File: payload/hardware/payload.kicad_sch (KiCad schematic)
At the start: 4 parts, among them J1 522071585, J2 Conn_01x05, U1 CM4102008, U3 CD74HC4067SM

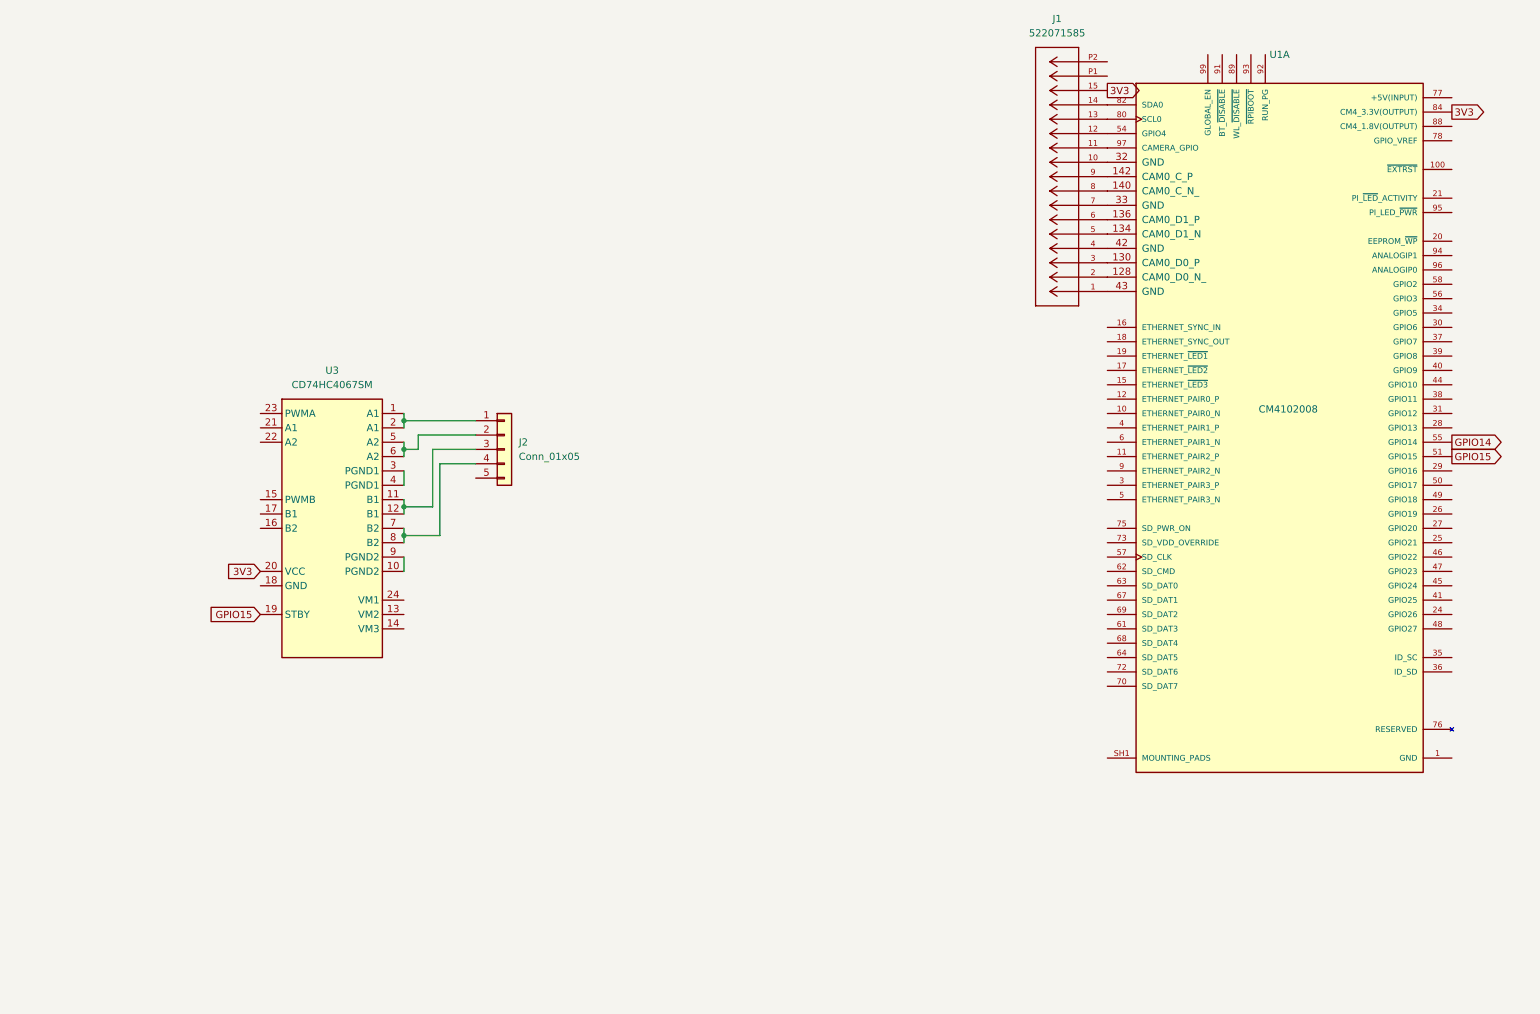
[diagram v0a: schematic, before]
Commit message: interboard connector and organization
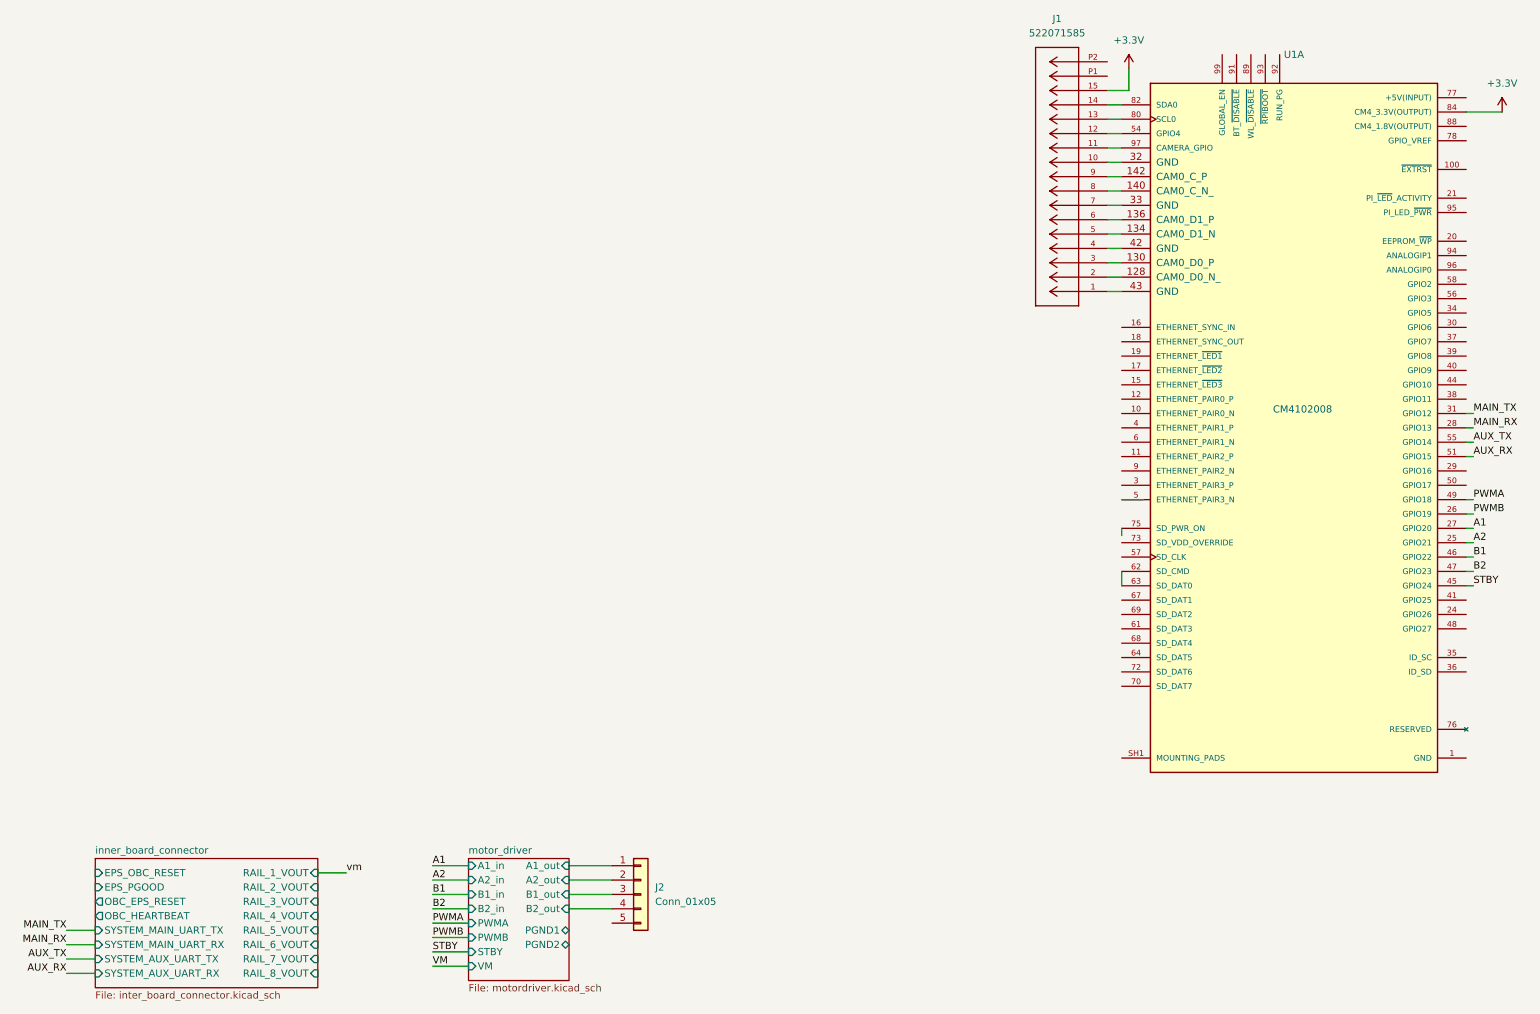
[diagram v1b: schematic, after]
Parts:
- removed U3: CD74HC4067SM, Package_SO:SSOP-24_5.3x8.2mm_P0.65mm, symbol 74xx:CD74HC4067SM
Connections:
- net motor_driver/A1_out: now reaches J2.1 (Pin_1)
- net motor_driver/B1_out: now reaches J2.3 (Pin_3)
- net motor_driver/A2_out: now reaches J2.2 (Pin_2)
- net motor_driver/B2_out: now reaches J2.4 (Pin_4)
- net A2: now reaches U1.25 (GPIO21)
- net PWMB: now reaches U1.26 (GPIO19)
- net A1: now reaches U1.27 (GPIO20)
- net MAIN_RX: now reaches U1.28 (GPIO13)
- net MAIN_TX: now reaches U1.31 (GPIO12)
- net STBY: now reaches U1.45 (GPIO24)
- net B1: now reaches U1.46 (GPIO22)
- net B2: now reaches U1.47 (GPIO23)
- net PWMA: now reaches U1.49 (GPIO18)
- net at U1.62 (SD_CMD): now also U1.63 (SD_DAT0)
- net CM4_3.3V(OUTPUT) renamed +3.3V
- net GPIO14 renamed AUX_TX
- net GPIO15 renamed AUX_RX
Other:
- added sheet inner_board_connector (inter_board_connector.kicad_sch)
- added sheet motor_driver (motordriver.kicad_sch)
- moved on the sheet: U1A

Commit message: create CM4 symbol
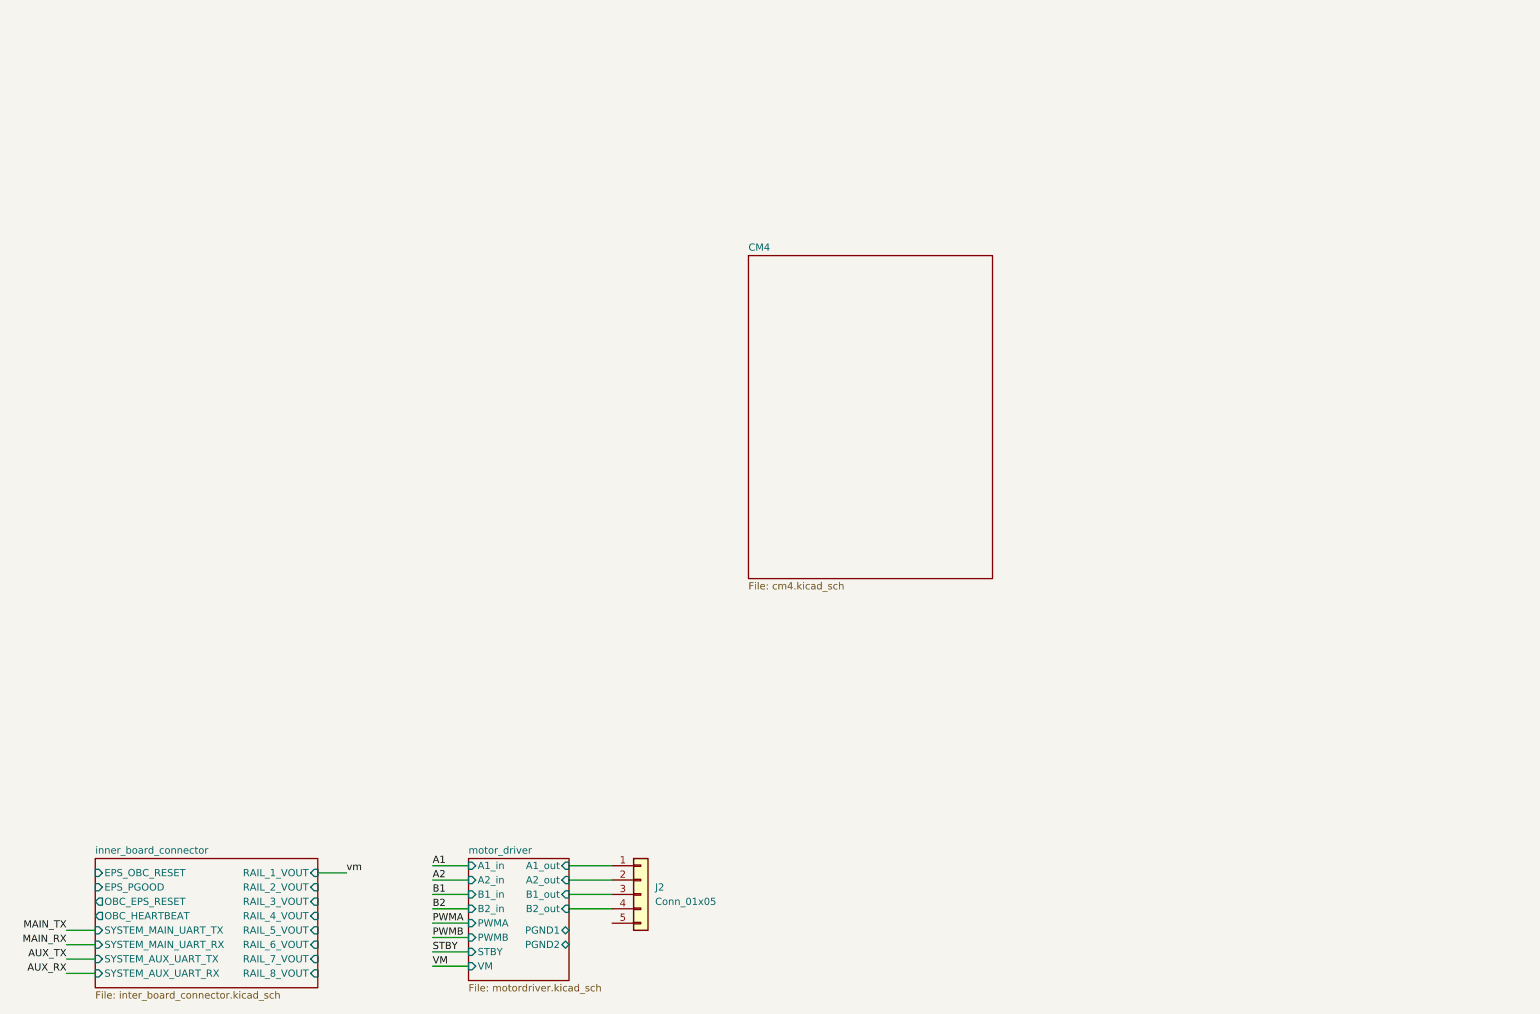
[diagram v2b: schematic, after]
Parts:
- removed J1: 522071585, footprints:CON_522071585_MOL, symbol 522071585:522071585
- removed U1: CM4102008, CM4102008:MODULE_CM4102008, symbol CM4102008:CM4102008
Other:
- added sheet CM4 (cm4.kicad_sch)

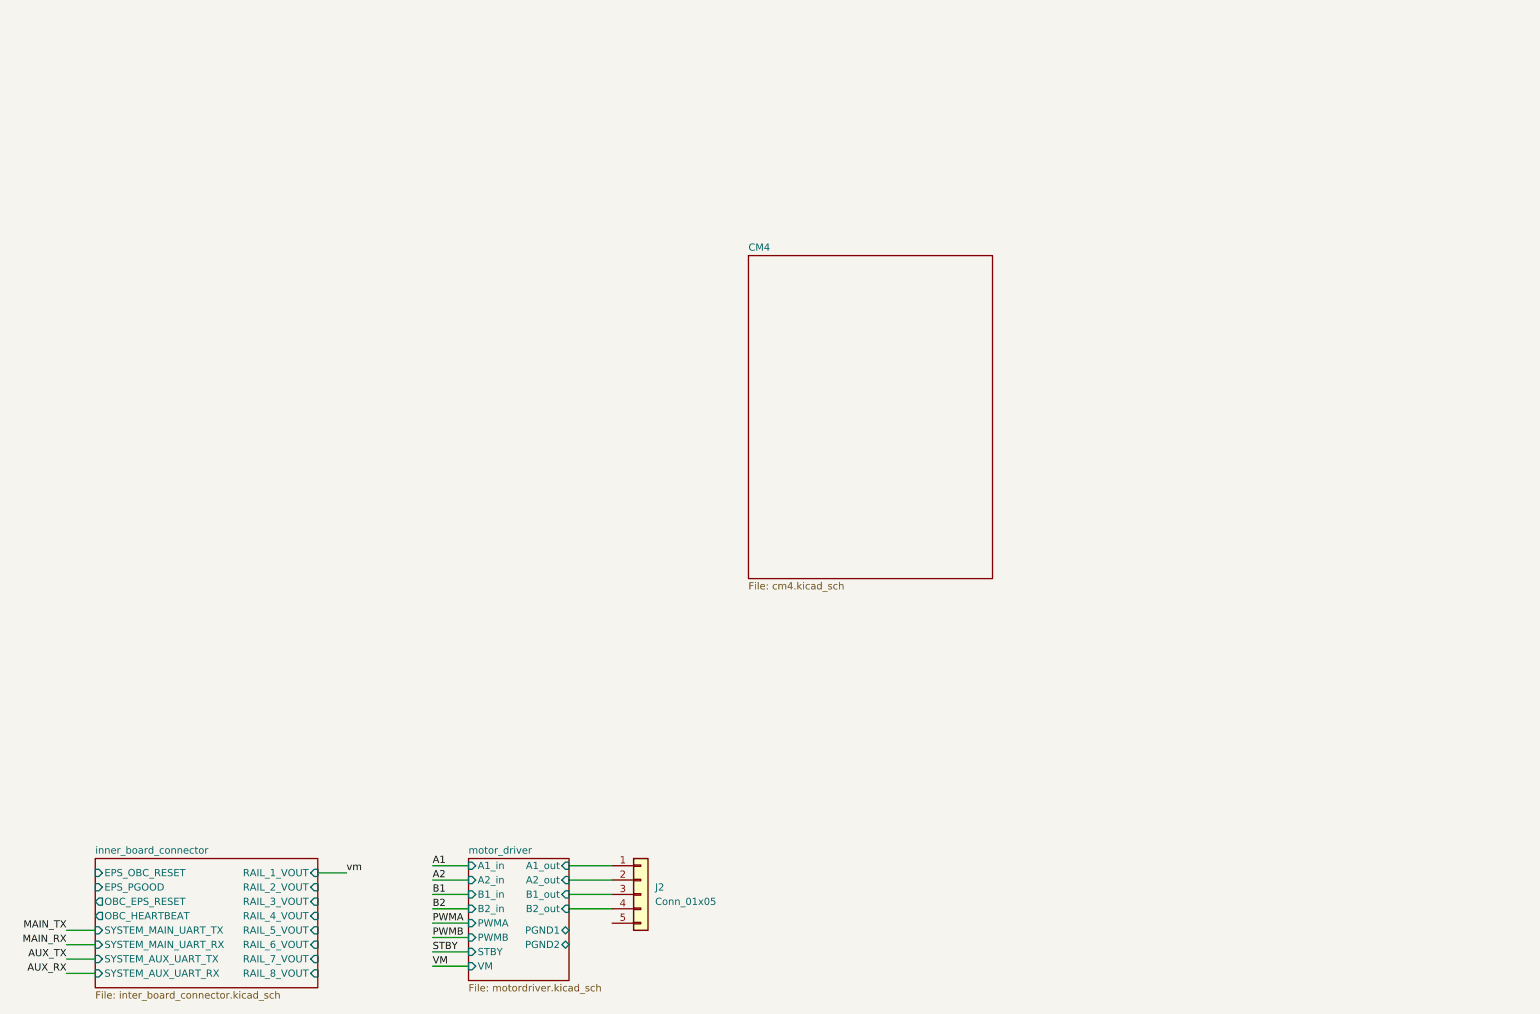
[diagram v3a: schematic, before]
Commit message: add ethernet
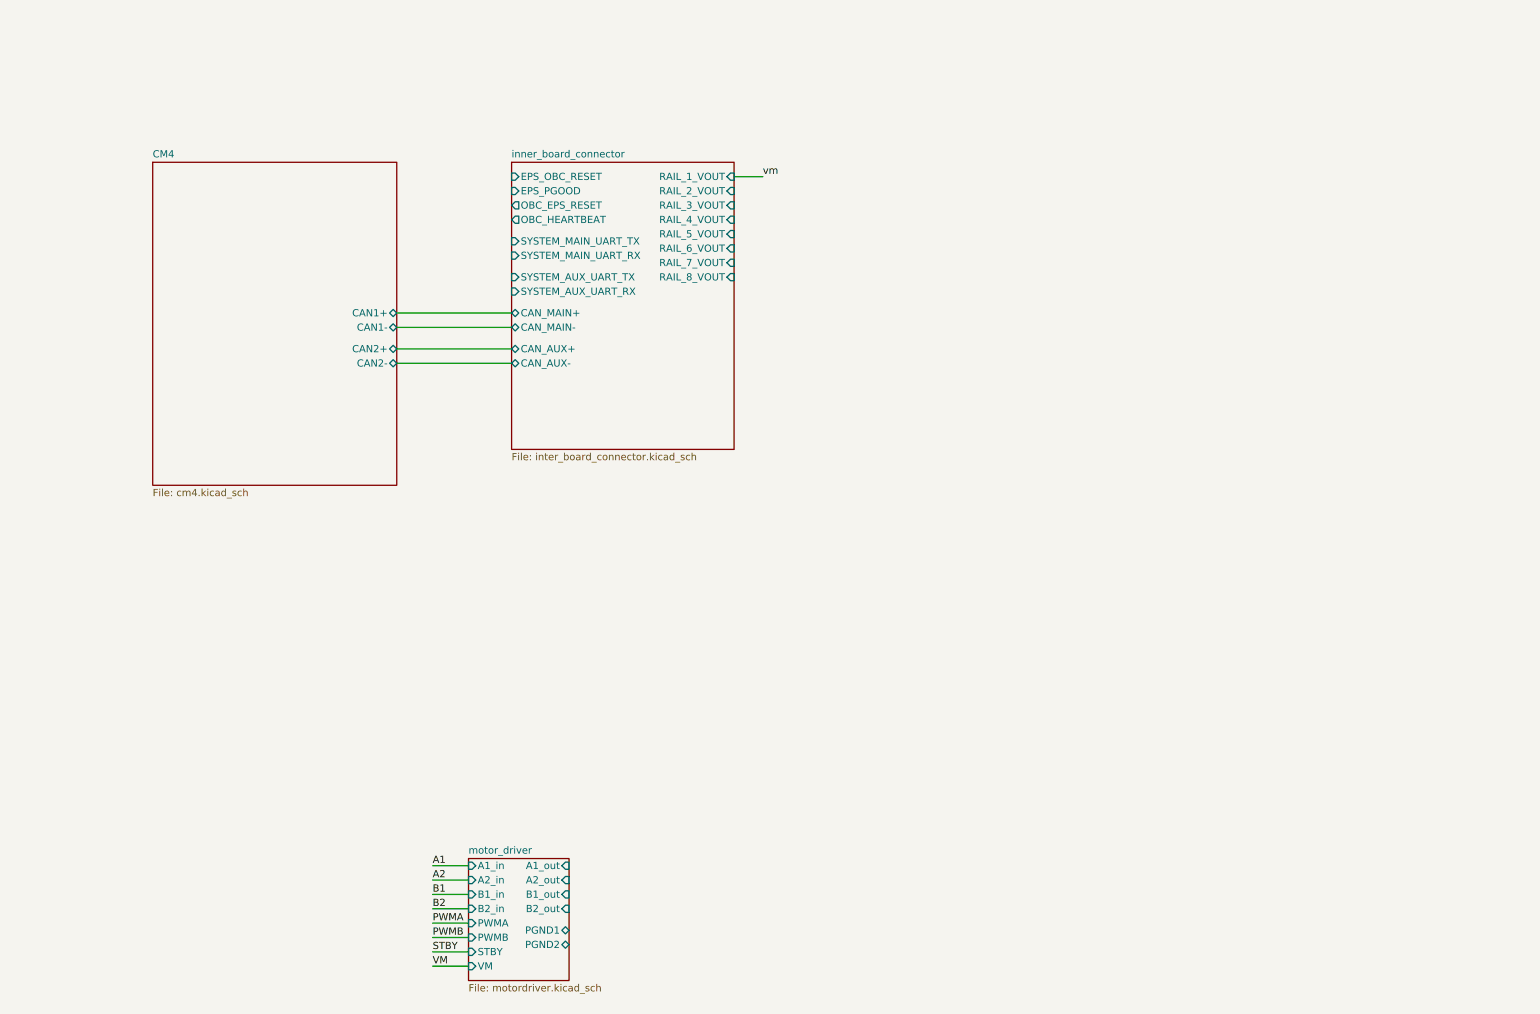
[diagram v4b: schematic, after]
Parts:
- removed J2: Conn_01x05, symbol Connector_Generic:Conn_01x05
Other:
- sheet CM4 ports: added CAN1+, CAN1-, CAN2+, CAN2-; removed none
- sheet inner_board_connector ports: added CAN_AUX+, CAN_AUX-, CAN_MAIN+, CAN_MAIN-; removed none

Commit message: motor driver schematic, work on high speed routing
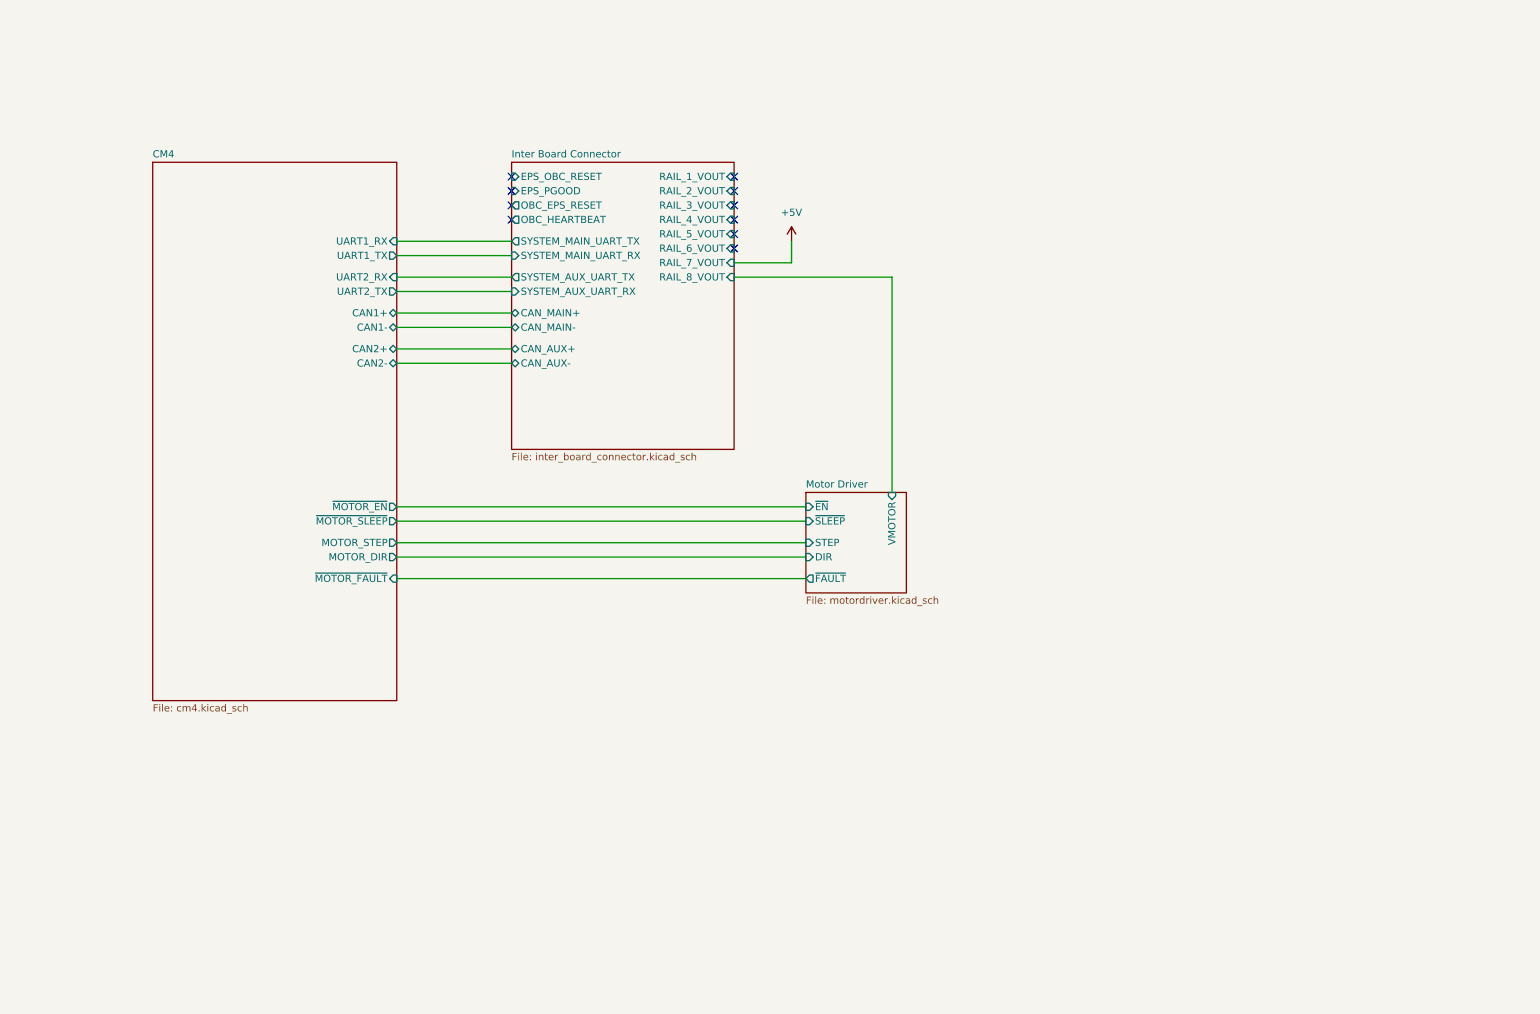
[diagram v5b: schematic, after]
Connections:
- no-connect marks 0 -> 10
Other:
- sheet inner_board_connector renamed Inter Board Connector
- sheet motor_driver renamed Motor Driver
- sheet CM4 ports: added MOTOR_DIR, MOTOR_STEP, UART1_RX, UART1_TX, UART2_RX, UART2_TX, ~{MOTOR_EN}, ~{MOTOR_FAULT}, ~{MOTOR_SLEEP}; removed none
- sheet Motor Driver ports: added DIR, STEP, VMOTOR, ~{EN}, ~{FAULT}, ~{SLEEP}; removed A1_in, A1_out, A2_in, A2_out, B1_in, B1_out, B2_in, B2_out, PGND1, PGND2, PWMA, PWMB, STBY, VM
